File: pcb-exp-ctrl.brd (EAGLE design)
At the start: 100 x 80 mm, 22 parts, among them IC1 SAA1064, IC2 TINY13-20PU, IC3 LP2950Z, K1 REED, T1 BC547, T2 BC547

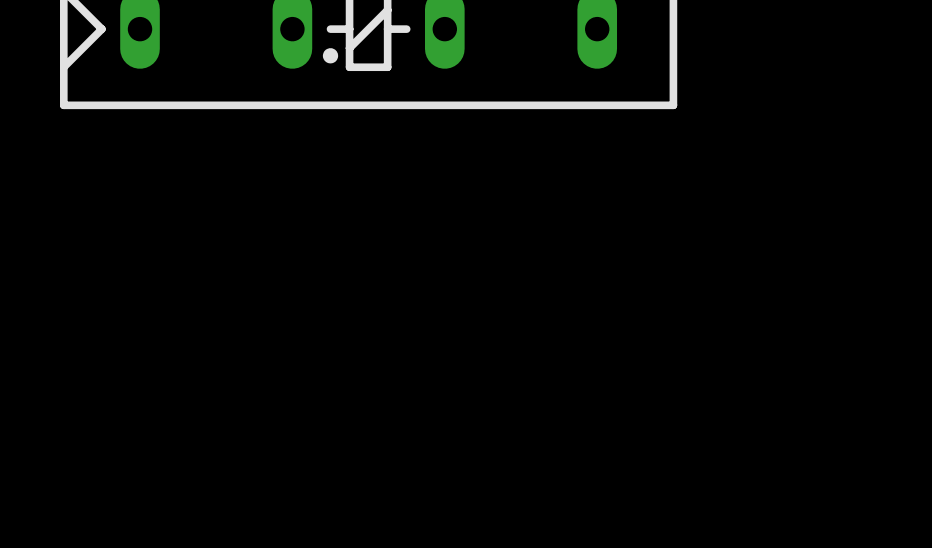
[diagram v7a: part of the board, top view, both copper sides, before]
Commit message: extra LEDs korrekt verdrahtet
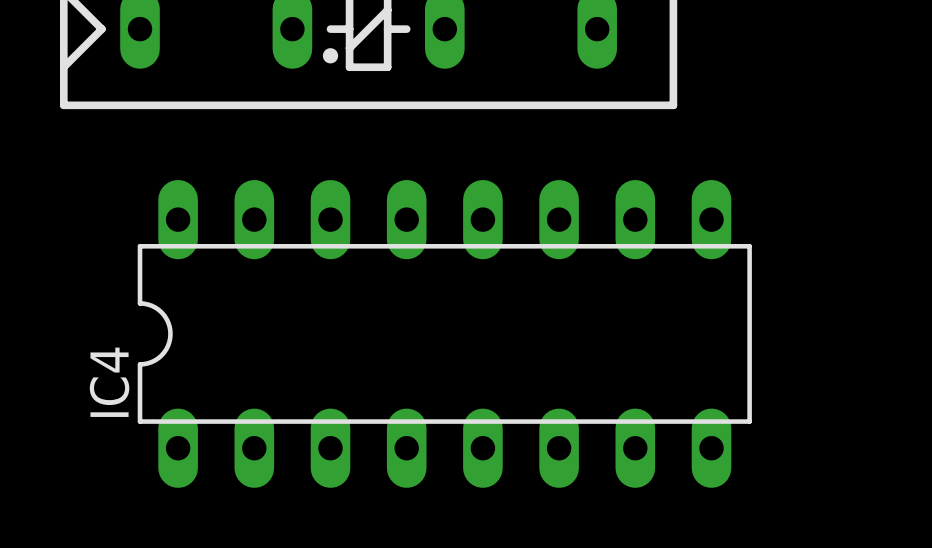
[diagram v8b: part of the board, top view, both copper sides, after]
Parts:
- added IC4: 74LS165N, 74xx-eu:DIL16
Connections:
- new net VCC: IC4.16
- net GND: now also IC4.8; no longer K1.1, K1.5
- net MISO: no longer K1.3
- net N$2: now also S1.+, S2.+, S3.+, S4.+
- net N$7: no longer S1.-, S2.-, S3.-, S4.-
- net P10: now also S2.-; no longer S2.+
- net P11: now also S3.-; no longer S3.+
- net P12: now also S4.-; no longer S4.+
- net P9: now also S1.-; no longer S1.+
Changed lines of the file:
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@@
 <attribute name="OC_FARNELL" value="unknown" x="-34.29" y="-72.39" size="1.778" layer="27" display="off"/>
 </element>
+<element name="IC4" library="74xx-eu" package="DIL16" value="74LS165N" x="-41.91" y="-80.01"/>
 </elements>
 <signals>
@@
 <contactref element="IC3" pad="2"/>
 <contactref element="C4" pad="-"/>
-<contactref element="K1" pad="5"/>
-<contactref element="K1" pad="1"/>
-<wire x1="-41.91" y1="-69.85" x2="-52.07" y2="-69.85" width="0" layer="19" extent="1-1"/>
-<wire x1="-36.83" y1="-53.34" x2="-41.91" y2="-69.85" width="0" layer="19" extent="1-1"/>
+<contactref element="IC4" pad="8"/>
+<wire x1="-36.83" y1="-53.34" x2="-33.02" y2="-83.82" width="0" layer="19" extent="1-1"/>
 <wire x1="-38.1" y1="-46.355" x2="-36.83" y2="-53.34" width="0" layer="19" extent="1-1"/>
 <wire x1="5.08" y1="-36.83" x2="-38.1" y2="-46.355" width="0" layer="19" extent="1-1"/>
@@
 <contactref element="IC1" pad="15"/>
 <contactref element="LED3" pad="7"/>
-<contactref element="S1" pad="+"/>
+<contactref element="S1" pad="-"/>
 <wire x1="27.94" y1="50.8" x2="38.1" y2="73.66" width="0" layer="19" extent="1-1"/>
-<wire x1="-7.62" y1="-29.21" x2="27.94" y2="50.8" width="0" layer="19" extent="1-1"/>
+<wire x1="-5.08" y1="-29.21" x2="27.94" y2="50.8" width="0" layer="19" extent="1-1"/>
 </signal>
 <signal name="P10">
 <contactref element="IC1" pad="16"/>
 <contactref element="LED3" pad="6"/>
-<contactref element="S2" pad="+"/>
+<contactref element="S2" pad="-"/>
 <wire x1="25.4" y1="50.8" x2="40.64" y2="73.66" width="0" layer="19" extent="1-1"/>
-<wire x1="-21.59" y1="-29.21" x2="25.4" y2="50.8" width="0" layer="19" extent="1-1"/>
+<wire x1="-19.05" y1="-29.21" x2="25.4" y2="50.8" width="0" layer="19" extent="1-1"/>
 </signal>
 <signal name="P11">
 <contactref element="IC1" pad="17"/>
 <contactref element="LED3" pad="4"/>
-<contactref element="S3" pad="+"/>
+<contactref element="S3" pad="-"/>
 <wire x1="22.86" y1="50.8" x2="38.1" y2="58.42" width="0" layer="19" extent="1-1"/>
-<wire x1="-35.56" y1="-29.21" x2="22.86" y2="50.8" width="0" layer="19" extent="1-1"/>
+<wire x1="-33.02" y1="-29.21" x2="22.86" y2="50.8" width="0" layer="19" extent="1-1"/>
 </signal>
 <signal name="P12">
 <contactref element="IC1" pad="18"/>
 <contactref element="LED3" pad="2"/>
-<contactref element="S4" pad="+"/>
-<wire x1="20.32" y1="50.8" x2="-49.53" y2="-50.8" width="0" layer="19" extent="1-1"/>
+<contactref element="S4" pad="-"/>
+<wire x1="20.32" y1="50.8" x2="-46.99" y2="-50.8" width="0" layer="19" extent="1-1"/>
 <wire x1="33.02" y1="58.42" x2="20.32" y2="50.8" width="0" layer="19" extent="1-1"/>
 </signal>
@@
 <contactref element="LED2" pad="3"/>
 <contactref element="T2" pad="1"/>
-<wire x1="22.86" y1="58.42" x2="22.86" y2="73.66" width="0" layer="19" extent="1-1"/>
-<wire x1="5.08" y1="-19.05" x2="22.86" y2="58.42" width="0" layer="19" extent="1-1"/>
+<contactref element="S4" pad="+"/>
+<contactref element="S3" pad="+"/>
+<contactref element="S2" pad="+"/>
+<contactref element="S1" pad="+"/>
+<wire x1="-35.56" y1="-29.21" x2="-49.53" y2="-50.8" width="0" layer="19" extent="1-1"/>
+<wire x1="-21.59" y1="-29.21" x2="-35.56" y2="-29.21" width="0" layer="19" extent="1-1"/>
+<wire x1="-7.62" y1="-29.21" x2="-21.59" y2="-29.21" width="0" layer="19" extent="1-1"/>
+<wire x1="5.08" y1="-19.05" x2="-7.62" y2="-29.21" width="0" layer="19" extent="1-1"/>
+<wire x1="22.86" y1="58.42" x2="5.08" y2="-19.05" width="0" layer="19" extent="1-1"/>
+<wire x1="22.86" y1="73.66" x2="22.86" y2="58.42" width="0" layer="19" extent="1-1"/>
 </signal>
 <signal name="SCK">
@@
 <contactref element="LED3" pad="3"/>
 <contactref element="T1" pad="1"/>
-<contactref element="S1" pad="-"/>
-<contactref element="S2" pad="-"/>
-<contactref element="S3" pad="-"/>
-<contactref element="S4" pad="-"/>
 <wire x1="35.56" y1="58.42" x2="35.56" y2="73.66" width="0" layer="19" extent="1-1"/>
 <wire x1="10.16" y1="73.66" x2="35.56" y2="73.66" width="0" layer="19" extent="1-1"/>
 <wire x1="10.16" y1="58.42" x2="10.16" y2="73.66" width="0" layer="19" extent="1-1"/>
 <wire x1="5.08" y1="-24.13" x2="10.16" y2="58.42" width="0" layer="19" extent="1-1"/>
-<wire x1="-5.08" y1="-29.21" x2="5.08" y2="-24.13" width="0" layer="19" extent="1-1"/>
-<wire x1="-19.05" y1="-29.21" x2="-5.08" y2="-29.21" width="0" layer="19" extent="1-1"/>
-<wire x1="-33.02" y1="-29.21" x2="-19.05" y2="-29.21" width="0" layer="19" extent="1-1"/>
-<wire x1="-46.99" y1="-50.8" x2="-33.02" y2="-29.21" width="0" layer="19" extent="1-1"/>
 </signal>
 <signal name="N$8">
@@
 <contactref element="IC2" pad="6"/>
 <contactref element="SV1" pad="1"/>
-<contactref element="K1" pad="3"/>
-<wire x1="38.1" y1="7.62" x2="-46.99" y2="-69.85" width="0" layer="19" extent="1-1"/>
-<wire x1="43.18" y1="50.8" x2="38.1" y2="7.62" width="0" layer="19" extent="1-1"/>
+<wire x1="38.1" y1="7.62" x2="43.18" y2="50.8" width="0" layer="19" extent="1-1"/>
 </signal>
 <signal name="+5V">
@@
 <wire x1="33.02" y1="50.8" x2="38.1" y2="50.8" width="0" layer="19" extent="1-1"/>
 </signal>
+<signal name="VCC">
+<contactref element="IC4" pad="16"/>
+</signal>
 </signals>
